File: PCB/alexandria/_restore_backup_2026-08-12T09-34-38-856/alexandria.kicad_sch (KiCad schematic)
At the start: 11 parts, among them IC1 ME6211C33M5G, J1 SJ2-35464B-SMT-TR, U1 ESP32-S3, U2 DFR0299, U3 TP4056_MICRO-USB_CHARGER_-_1A, U4 CR2013-MI2120

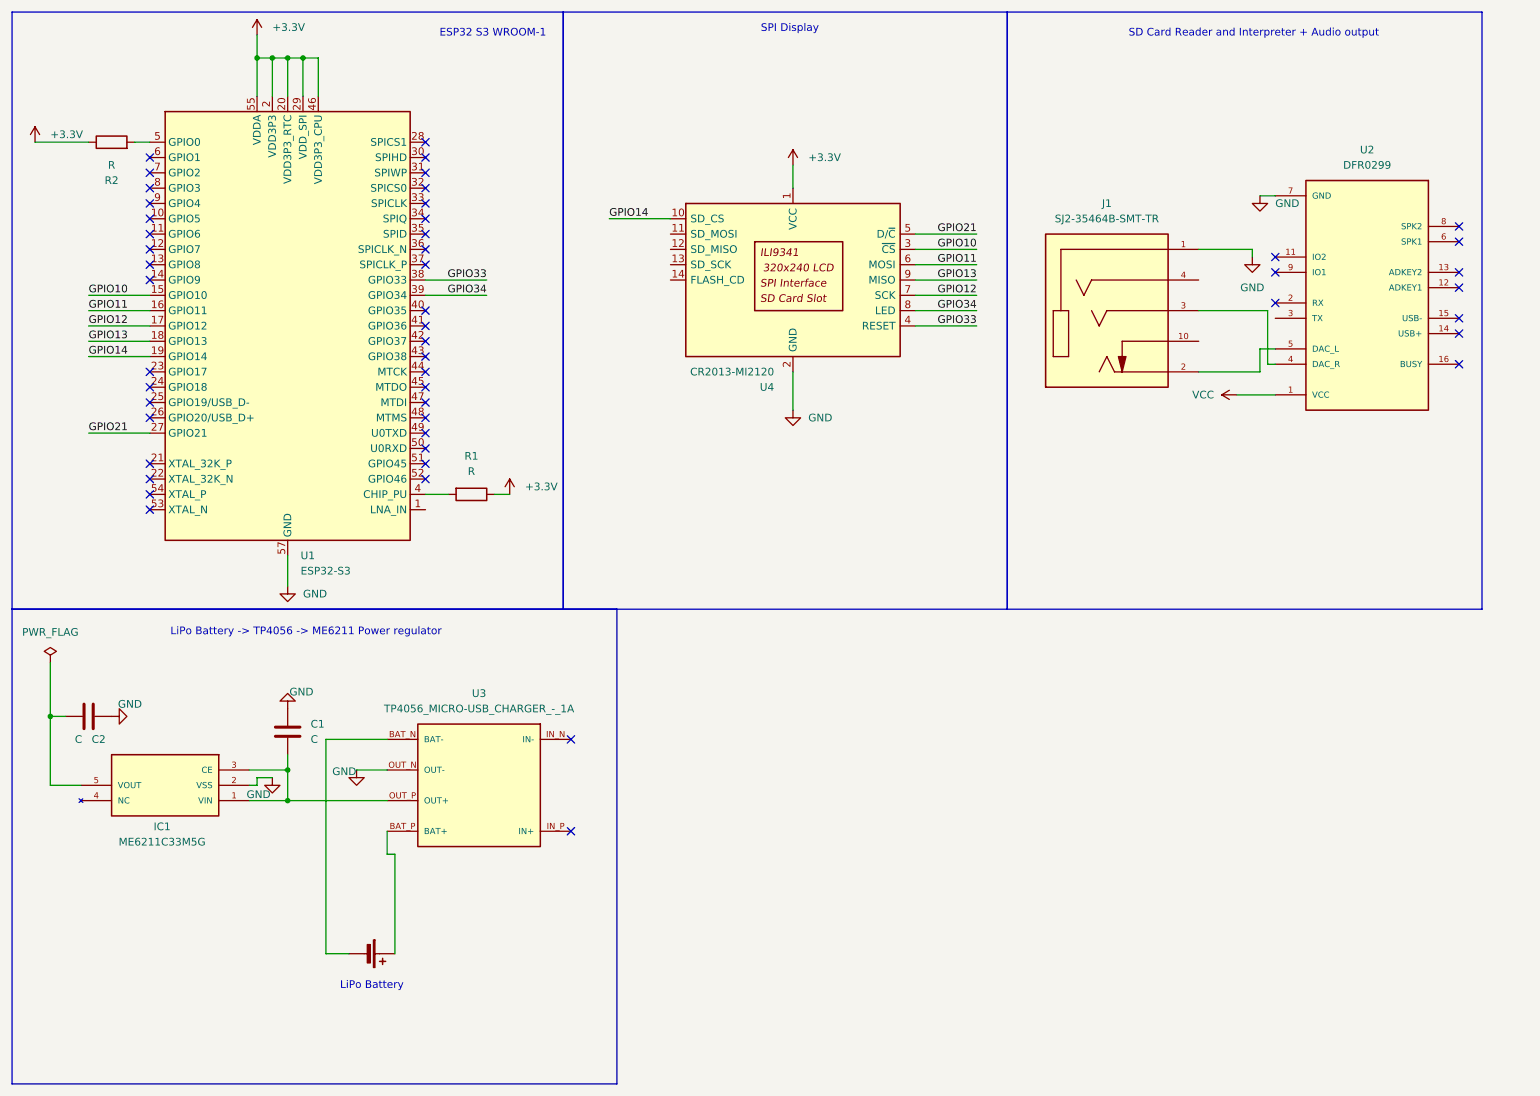
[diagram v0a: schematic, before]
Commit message: Almost complete the schematic. Use of other audio jack schematic. Complete clean-up of the parts in the schematic into sections.
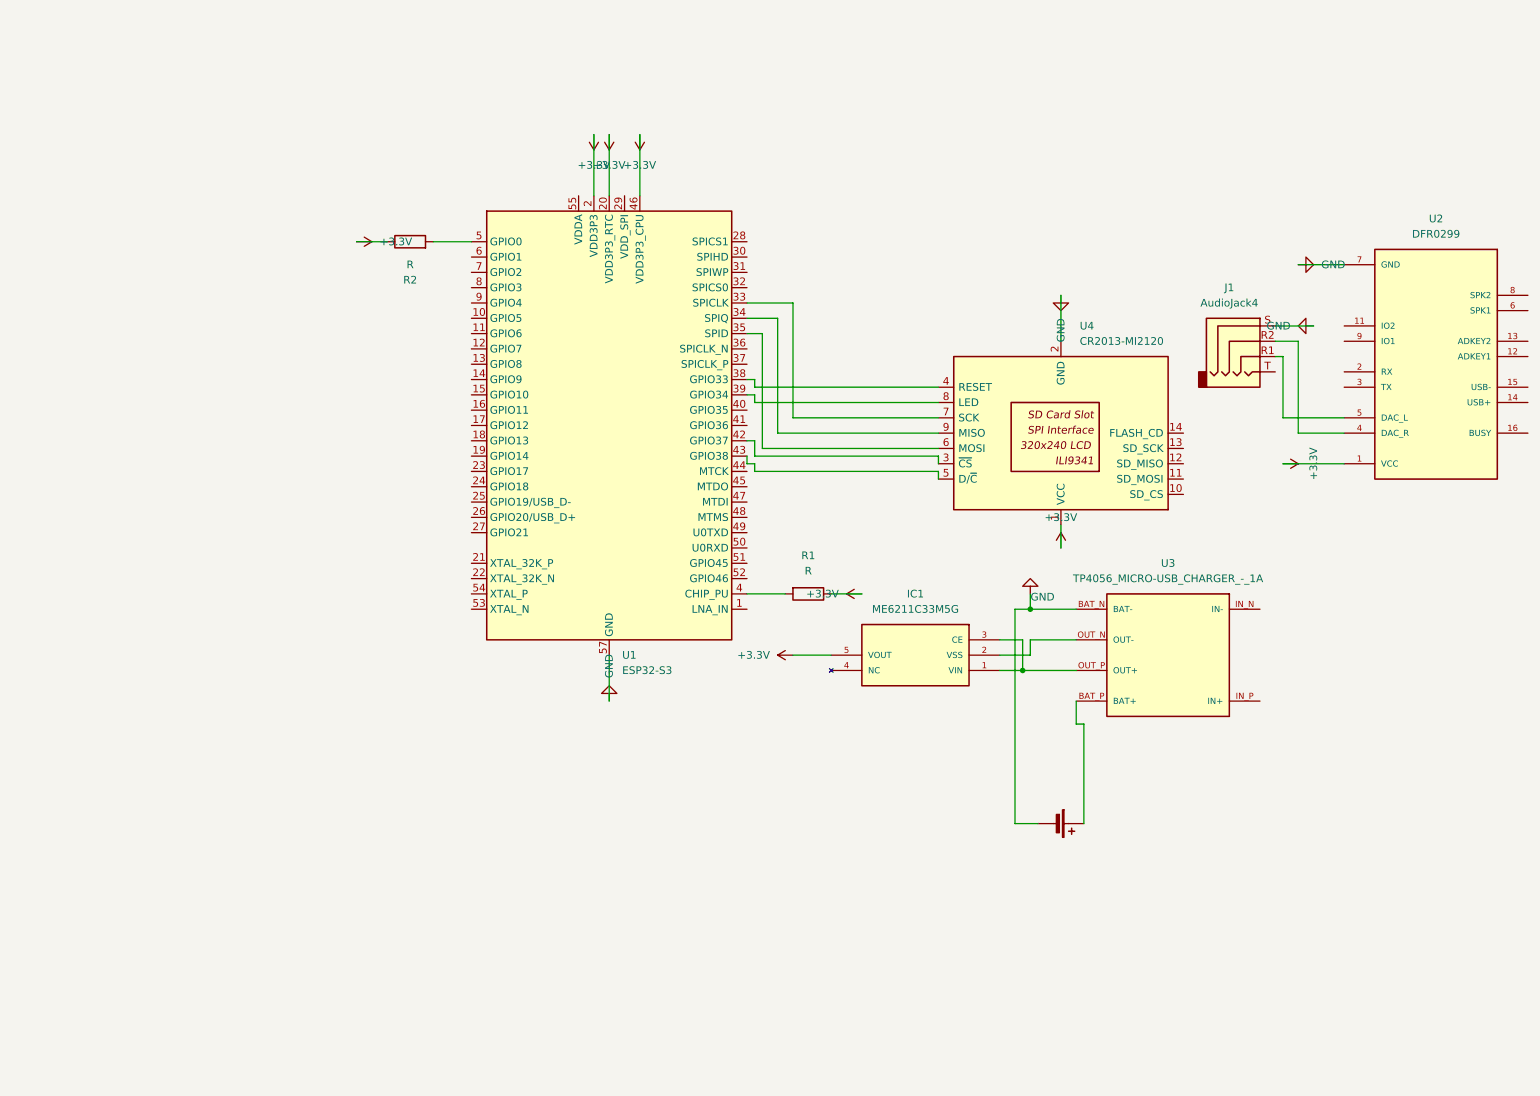
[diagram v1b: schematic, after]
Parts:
- removed C1, C2: C, symbol Device:C
- removed J1: SJ2-35464B-SMT-TR, SJ2-35464B-SMT-TR:CUI_SJ2-35464B-SMT-TR, symbol Kicad:SJ2-35464B-SMT-TR
- added J1: AudioJack4, symbol Connector_Audio:AudioJack4
- IC1: footprint Alexandria:SOT95P282X145-5N -> ME6211C33M5G:SOT95P282X145-5N
- U2: footprint Alexandria:MODULE_DFR0299 -> DFR0299:MODULE_DFR0299
- U4: footprint Alexandria:ILI9341 -> Display:CR2013-MI2120
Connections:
- net VCC is gone; now on net +3.3V: U2.1 (VCC)
- net +3.3V: now also IC1.5 (VOUT); no longer U1.29 (VDD_SPI), U1.55 (VDDA), U1.56 (VDDA)
- net GND: now also BT1.2 (-), U3.BAT_N (BAT-), J1.S; no longer IC1.2 (VSS), U3.OUT_N (OUT-)
- net at U2.5 (DAC_L): now also J1.R1
- net at U2.4 (DAC_R): now also J1.R2
- net at U1.33 (SPICLK): now also U4.7 (SCK)
- net at U1.34 (SPIQ): now also U4.9 (MISO)
- net at U1.35 (SPID): now also U4.6 (MOSI)
- net at U1.42 (GPIO37): now also U4.3 (~{CS})
- net at U1.43 (GPIO38): now also U4.5 (D/~{C})
- net GPIO10: no longer names the net of U1.15 (GPIO10)
- net GPIO10: no longer U4.3 (~{CS})
- net GPIO11: no longer names the net of U1.16 (GPIO11)
- net GPIO11: no longer U4.6 (MOSI)
- net GPIO12: no longer names the net of U1.17 (GPIO12)
- net GPIO12: no longer U4.7 (SCK)
- net GPIO13: no longer names the net of U1.18 (GPIO13)
- net GPIO13: no longer U4.9 (MISO)
- net GPIO14: no longer names the net of U1.19 (GPIO14)
- net GPIO14: no longer U4.10 (SD_CS)
- net GPIO21: no longer names the net of U1.27 (GPIO21)
- net GPIO21: no longer U4.5 (D/~{C})
- net GPIO33: no longer names the net of U1.38 (GPIO33), U4.4 (RESET)
- net GPIO34: no longer names the net of U1.39 (GPIO34), U4.8 (LED)
- new net: IC1.2 (VSS), U3.OUT_N (OUT-)
- new net: U1.55 (VDDA), U1.56 (VDDA)
- no-connect marks 50 -> 0
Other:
- note removed: "ESP32 S3 WROOM-1"
- note removed: "LiPo Battery"
- note removed: "LiPo Battery -> TP4056 -> ME6211 Power regulator"
- note removed: "SD Card Reader and Interpreter + Audio output"
- note removed: "SPI Display"
- moved on the sheet: IC1, R1, R2, U1, U2, U3, U4
